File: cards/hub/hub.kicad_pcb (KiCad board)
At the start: 2 copper layers, 100 x 100 mm, 29 parts, among them J1 BENCH +5V, J2 BENCH GND, J3 BUS, J4 BUS

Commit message: The bus headers go on the back of all 26 boards, no track moved; the silkscreen refitted (D059, D062)
An IDC socket lies across its ribbon, so the ribbon could never run along a
row of cards as drawn. It runs behind them, and the 64-pin headers are
soldered on the back. This commit is that move, made in place on the routed
boards: no board was routed again.

How the header sits (D062): in the holes it had, turned over top to bottom,
notch toward the top edge. A pin of the odd row is then in the hole its even
neighbour had, so the two signals of every pair of pins change places: CLK
is pin 6, RST pin 8, +5V pins 1, 2 and 64. bus.py keeps both tables: PINS,
what the header's pins carry, and HOLES, what the copper was routed to.

The proof, on all 26 boards against 992a90f (sim/board_diff.py):
  netlist the same, element for element; every track, every via and every
  hole the same; each copper and mask layer differs by two pad shapes per
  header (pin 1's square went to the hole beside it, both on +5V) and the
  ground pour's outline round those two pads, nowhere else by more than a
  tenth of a micrometre.
sim/rebuild_check.py runs every builder into a scratch directory: each
writes the plan and the netlist that are committed, so a rebuild gives
this board. order_check.py --machine holds every pad of the 27 headers to
bus.py and requires them on the back.

What the move costs: on the ribbon RST had a ground conductor on both
sides; now one neighbour is BUS1#. tb_rst_neighbour.py puts the two lines
on the bench with every gate the routed boards hang on them: RST rises
0.28 to 0.43 V when BUS1# is released, against a lowest threshold of 0.8 V
(sim/results/rst_neighbour.md). The machine deck's crosstalk option now
couples the pins that are neighbours on the ribbon; the crosstalk stage of
the machine gate has to be run again on that order.

Silkscreen (pcb.fit_silk): every label to 1.0 mm where it has room, off
pads, vias, outlines and other labels, out from under the pa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
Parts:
- J3, J4: moved to B.Cu
- moved J4 2.54 mm to (10.6, 90.5), turned to -90 degrees
- moved J3 2.54 mm to (10.6, 4.96), turned to -90 degrees
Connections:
- J3 pad 10: BUS1# -> BUS0#
- J3 pad 11: BUS2# -> BUS3#
- J3 pad 12: BUS3# -> BUS2#
- J3 pad 13: A0 -> A1
- J3 pad 14: A1 -> A0
- J3 pad 15: A2 -> A3
- J3 pad 16: A3 -> A2
- J3 pad 17: B0 -> B1
- J3 pad 18: B1 -> B0
- J3 pad 19: B2 -> B3
- J3 pad 20: B3 -> B2
- J3 pad 21: PC0 -> PC1
- J3 pad 22: PC1 -> PC0
- J3 pad 23: PC2 -> PC3
- J3 pad 24: PC3 -> PC2
- J3 pad 25: PC4 -> PC5
- J3 pad 26: PC5 -> PC4
- J3 pad 27: PC6 -> PC7
- J3 pad 28: PC7 -> PC6
- J3 pad 29: M0 -> M1
- J3 pad 30: M1 -> M0
- J3 pad 31: M2 -> M3
- J3 pad 32: M3 -> M2
- J3 pad 33: M4 -> M5
- J3 pad 34: M5 -> M4
- J3 pad 35: M6 -> M7
- J3 pad 36: M7 -> M6
- J3 pad 37: CF -> ZF
- J3 pad 38: ZF -> CF
- J3 pad 39: SUB -> EO
- J3 pad 40: EO -> SUB
- J3 pad 41: AI -> AO
- J3 pad 42: AO -> AI
- J3 pad 43: BI -> BO
- J3 pad 44: BO -> BI
- J3 pad 45: BA -> AB
- J3 pad 46: AB -> BA
- J3 pad 47: OI -> IO
- J3 pad 48: IO -> OI
- J3 pad 49: II -> PCE
- J3 pad 5: CLK -> GND
- J3 pad 50: PCE -> II
- J3 pad 51: PCL -> FI
- J3 pad 52: FI -> PCL
- J3 pad 53: HLT -> MAI
- J3 pad 54: MAI -> HLT
- J3 pad 55: MI -> MO
- J3 pad 56: MO -> MI
- J3 pad 57: WRL -> WRH
- J3 pad 58: WRH -> WRL
- J3 pad 59: ONE -> F0
- J3 pad 6: GND -> CLK
- J3 pad 60: F0 -> ONE
- J3 pad 61: F1 -> INP
- J3 pad 62: INP -> F1
- J3 pad 63: +5V -> GND
- J3 pad 64: GND -> +5V
- J3 pad 7: RST -> GND
- J3 pad 8: GND -> RST
- J3 pad 9: BUS0# -> BUS1#
- J4 pad 10: BUS1# -> BUS0#
- J4 pad 11: BUS2# -> BUS3#
- J4 pad 12: BUS3# -> BUS2#
- J4 pad 13: A0 -> A1
- J4 pad 14: A1 -> A0
- J4 pad 15: A2 -> A3
- J4 pad 16: A3 -> A2
- J4 pad 17: B0 -> B1
- J4 pad 18: B1 -> B0
- J4 pad 19: B2 -> B3
- J4 pad 20: B3 -> B2
- J4 pad 21: PC0 -> PC1
- J4 pad 22: PC1 -> PC0
- J4 pad 23: PC2 -> PC3
- J4 pad 24: PC3 -> PC2
- J4 pad 25: PC4 -> PC5
- J4 pad 26: PC5 -> PC4
- J4 pad 27: PC6 -> PC7
- J4 pad 28: PC7 -> PC6
- J4 pad 29: M0 -> M1
- J4 pad 30: M1 -> M0
- J4 pad 31: M2 -> M3
- J4 pad 32: M3 -> M2
- J4 pad 33: M4 -> M5
- J4 pad 34: M5 -> M4
- J4 pad 35: M6 -> M7
- J4 pad 36: M7 -> M6
- J4 pad 37: CF -> ZF
- J4 pad 38: ZF -> CF
- J4 pad 39: SUB -> EO
- J4 pad 40: EO -> SUB
- J4 pad 41: AI -> AO
- J4 pad 42: AO -> AI
- J4 pad 43: BI -> BO
- J4 pad 44: BO -> BI
- J4 pad 45: BA -> AB
- J4 pad 46: AB -> BA
- J4 pad 47: OI -> IO
- J4 pad 48: IO -> OI
- J4 pad 49: II -> PCE
- J4 pad 5: CLK -> GND
- J4 pad 50: PCE -> II
- J4 pad 51: PCL -> FI
- J4 pad 52: FI -> PCL
- J4 pad 53: HLT -> MAI
- J4 pad 54: MAI -> HLT
- J4 pad 55: MI -> MO
- J4 pad 56: MO -> MI
- J4 pad 57: WRL -> WRH
- J4 pad 58: WRH -> WRL
- J4 pad 59: ONE -> F0
- J4 pad 6: GND -> CLK
- J4 pad 60: F0 -> ONE
- J4 pad 61: F1 -> INP
- J4 pad 62: INP -> F1
- J4 pad 63: +5V -> GND
- J4 pad 64: GND -> +5V
- J4 pad 7: RST -> GND
- J4 pad 8: GND -> RST
- J4 pad 9: BUS0# -> BUS1#
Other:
- board text added: "2"
- board text added: "63"
- board text added: "64"
- board text added: "HEADER HERE"
- board text added: "HEADER ON THE BACK"
- board text added: "NOTCH TO TOP"

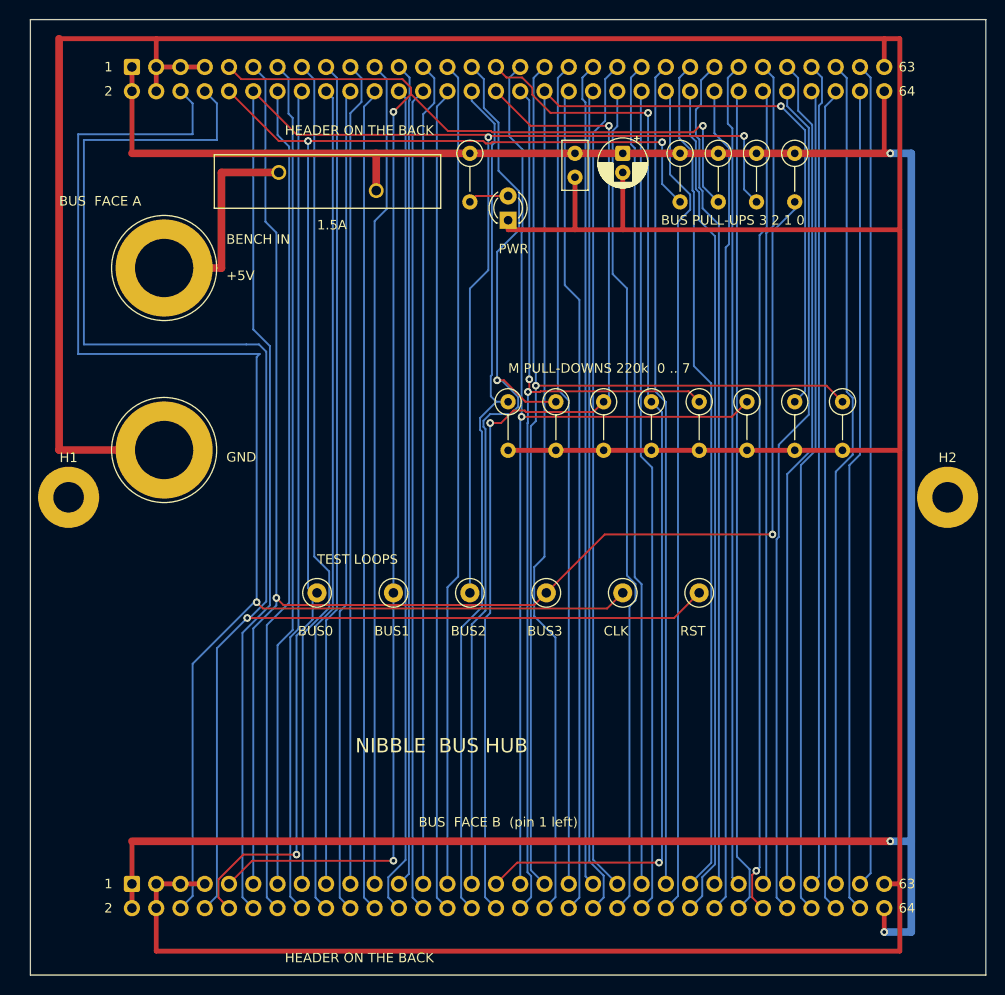
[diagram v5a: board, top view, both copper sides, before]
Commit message: Hub: sockets that are soldered in, and the crowbar (D061, D063)
The hub was on hold for two reasons, and gets the protection that was
decided while it waited.

Sockets. The panel sockets of D058 put a bushing, a nut and a solder tag
15 mm behind the board, where the frame's rail is. The new ones are Cal Test
CT3151V1 (red -2, black -0): they stand on the board on four solder pins
with 1.6 mm behind it. The footprint is drawn from the maker's drawing
(P315100 rev H, sheet 3: four 1.60 mm holes on a 4.76 mm diamond, body
13.5 mm) and lives in lib/nibble.pretty; KiCad's own CT3151 footprint is the
one that lies on its side. The keep-outs and the hand-led CLK and RST of
the nut's time are gone.

Crowbar, five parts behind the polyfuse: 1N4735A (6.2 V) into the gate of a
BT151-500R across the rail, 100 ohm and 100 nF on the gate, a 1N5408 across
the rail the other way round. The values are the bench's
(sim/results/crowbar.md). The loop that carries the supply's limit once it
has fired (socket, fuse, SCR, socket) is 2 mm copper. The SCR's tab faces the
fuse, with room above it for a clip-on heatsink.

The first placement had the gate's three parts behind the cathode's track
and the router left one net open in three attempts; on the gate pin's side
it routes in one. The crowbar's parts are created last, so every part that
is in the machine's simulation keeps its reference: the hub's SPICE export
is the same line for line.

The gate's pins rule knows the three new parts (an SCR across the rail with
its gate on neither; a zener and a diode that stand against the rail on
purpose) and is tested on eight more made-up faults. On the hub as built:
every check passes but `clean`, which is this commit.

Co-Authored-By: Claude Fable 5.1 <noreply@anthropic.com>
Claude-Session: https://claude.ai/code/session_01RktbhdQjDu7SpFpvkevyUU
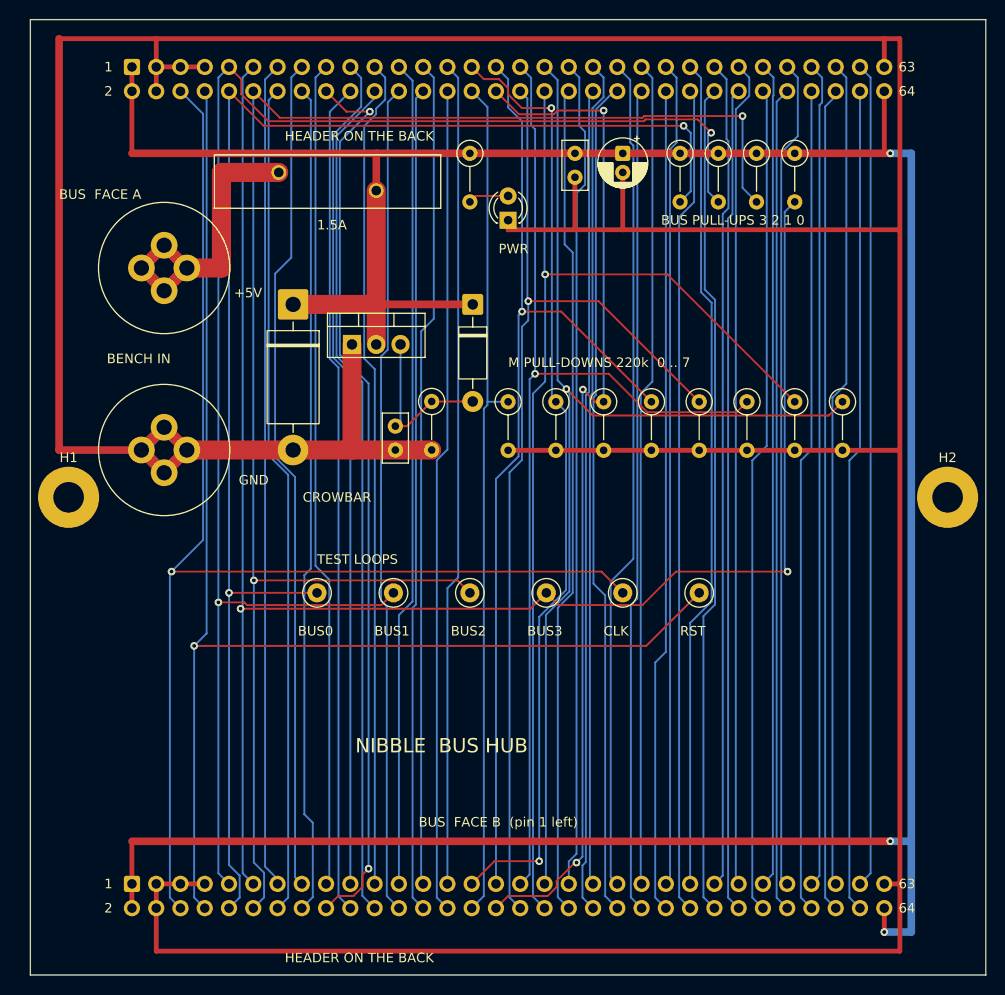
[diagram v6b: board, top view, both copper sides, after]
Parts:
- added C3: 100n, C_Disc_D5.0mm_W2.5mm_P2.50mm, F.Cu at (38.2, 42.5)
- added D2: 1N4735A, D_DO-41_SOD81_P10.16mm_Horizontal, F.Cu at (46.3, 29.8)
- added D3: 1N5408, D_DO-201AD_P15.24mm_Horizontal, F.Cu at (27.5, 29.8)
- added Q1: BT151-500R, TO-220-3_Vertical, F.Cu at (33.7, 34.0)
- added R14: 100, R_Axial_DIN0207_L6.3mm_D2.5mm_P5.08mm_Vertical, F.Cu at (42.0, 40.0)
- J1, J2: footprint Banana_Jack_1Pin -> Banana_CalTest_CT3151V1_Vertical
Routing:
- net GND: track 457.2 -> 532.2 mm
- net +5V: track 285.4 -> 338.1 mm
- net RST: track 169.8 -> 141.7 mm
- net M6: track 145.2 -> 118.2 mm
- net BUS2#: track 197.3 -> 171.6 mm
- net VBUS: track 22.0 -> 46.5 mm
- net CLK: track 159.9 -> 136.5 mm
- net Net-(D2-A): track 0.00 -> 17.9 mm
- net M3: track 115.5 -> 105.2 mm, vias 2 -> 1
- net BUS0#: track 143.4 -> 153.4 mm, vias 3 -> 2
- net BUS3#: track 178.6 -> 185.8 mm
- net B0: track 87.0 -> 94.1 mm, vias 0 -> 2
- net BUS1#: track 160.9 -> 167.6 mm, vias 3 -> 2
- net M4: track 105.0 -> 109.4 mm, vias 2 -> 1
- net PC0: track 86.4 -> 88.8 mm
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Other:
- board text added: "CROWBAR"

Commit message: Hub: an empty spot for the RST capacitor, so the fallback is a part and not leads on header pins
C-RST beside the RST test loop: pads for a 2.5 mm disc between RST and
ground, do-not-populate, in no parts list and not in the simulation (the
hub's export is the same, line for line, sorted). The simulation says the
pickup on RST stays at 0.3 to 0.4 V, under the 0.6 V it may
(rst_neighbour.md); if the scope says more, 2.2 nF goes here. Routed
again with freerouting 2.4.1, DRC clean, 0 unconnected, labels 1.0 mm.

Order gate: headers() reads a board's connectors in reference order; the
file's order shuffles on a rebuild and the self-test's planted fault on
the hub's second header went looking for a key that had moved.

bring-up.md section 9 and cards/README.md point at the spot.

Co-Authored-By: Claude Fable 5.1 <noreply@anthropic.com>
Claude-Session: https://claude.ai/code/session_01RktbhdQjDu7SpFpvkevyUU
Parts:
- added C4: 100n, C_Disc_D5.0mm_W2.5mm_P2.50mm, F.Cu at (38.2, 42.5)
- C3: value 100n -> 2.2n
- moved C3 43.5 mm to (78.0, 60.0), turned to 0 degrees
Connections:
- C3 pad 1: Net-(D2-A) -> RST
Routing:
- net GND: track 532.2 -> 557.8 mm
- net RST: track 141.7 -> 149.7 mm
- net MI: track 86.4 -> 87.1 mm
- net MO: track 86.9 -> 87.5 mm
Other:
- board text added: "C-RST"
- board text added: "FIT IF NEEDED"

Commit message: Silk: the front no longer says HEADER ON THE BACK; the back says HEADER HERE, which is enough
A "not here" note under the holes on every board, the kind of text that
narrates instead of naming. The back carries the header's outline with
HEADER HERE and NOTCH TO TOP; the front keeps the pin numbers 1, 2, 63,
64. All 26 boards re-silked in place from their plans (no re-route, the
schematics untouched); the order gate's silk rule now wants HEADER HERE
on the back and no HEADER ON THE BACK anywhere. Gate all pass, every
builder writes what is committed, parts tables unchanged.

Co-Authored-By: Claude Fable 5.1 <noreply@anthropic.com>
Claude-Session: https://claude.ai/code/session_01RktbhdQjDu7SpFpvkevyUU
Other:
- board text removed: "HEADER ON THE BACK"
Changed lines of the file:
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@@
-		)
-	)
-	(gr_text "HEADER ON THE BACK"
-		(at 26.63 12.2 0)
-		(layer "F.SilkS")
-		(effects
-			(font
-				(size 1 1)
-				(thickness 0.15)
-			)
-			(justify left)
-		)
-	)
-	(gr_text "HEADER ON THE BACK"
-		(at 26.63 98.2 0)
-		(layer "F.SilkS")
-		(effects
-			(font
-				(size 1 1)
-				(thickness 0.15)
-			)
-			(justify left)
 		)
 	)
